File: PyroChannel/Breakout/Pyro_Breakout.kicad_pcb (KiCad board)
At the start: 2 copper layers, 40.6 x 63.5 mm, 17 parts, among them J101 Conn_01x02, J102 Conn_01x05, J103 Conn_01x02, J301 Conn_01x02_Female, J401 Conn_01x02_Female, Q201 IRLML6344TRPBFee, Q301 IRLML6344TRPBFee, Q302 IRLML6344TRPBFee, Q401 IRLML6344TRPBFee, Q402 IRLML6344TRPBFee

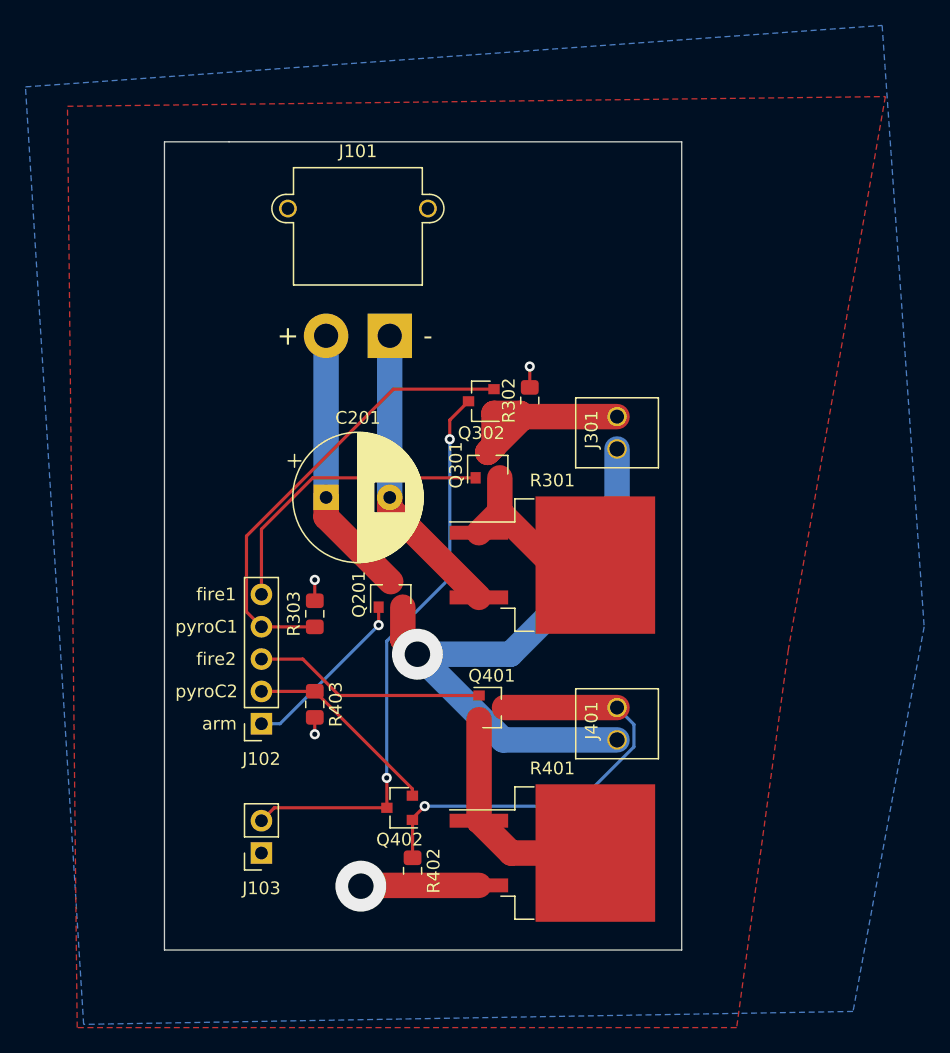
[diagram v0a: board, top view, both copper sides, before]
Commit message: Updated Heirarchichal schematics and breakout to fix checkPyro error
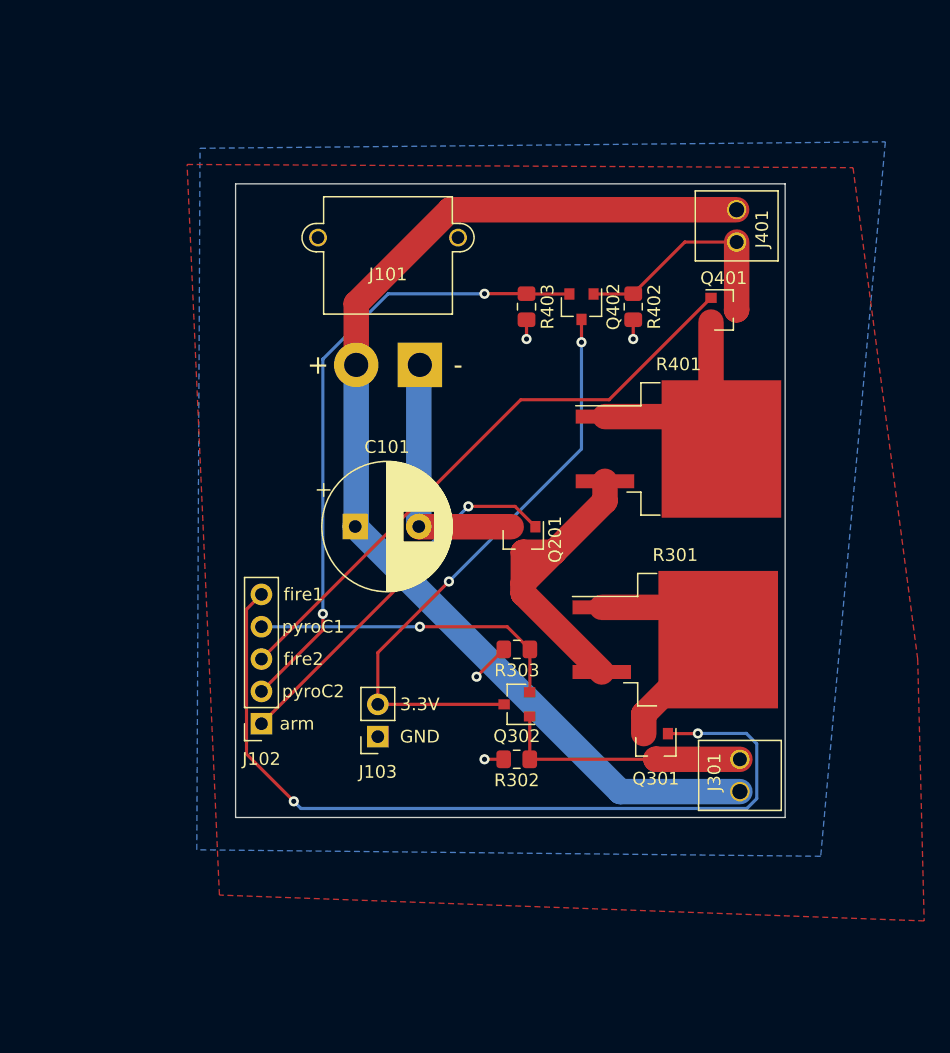
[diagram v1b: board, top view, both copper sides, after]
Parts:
- removed C201: 1mF, PyroChannel:CP_Radial_D10.0mm_P5.00mm
- added C101: 1mF, PyroChannel:CP_Radial_D10.0mm_P5.00mm, F.Cu at (111.5, 75.9)
- moved R402 47.6 mm to (133.3, 58.7)
- moved Q402 41.9 mm to (129.3, 58.7), turned to 270 degrees
- moved J401 40.2 mm to (141.5, 52.3), turned to 270 degrees
- moved Q401 36.2 mm to (140.5, 58.9)
- moved R403 35.4 mm to (125.0, 58.7)
- moved R401 33.3 mm to (136.9, 69.8)
- moved J301 28.6 mm to (141.7, 95.5)
- moved R302 28.2 mm to (124.2, 94.2), turned to 180 degrees
- moved Q301 25.7 mm to (135.1, 93.2), turned to 270 degrees
- moved Q302 24.0 mm to (124.2, 89.9)
- moved R303 16.1 mm to (124.2, 85.6), turned to 180 degrees
- moved J103 12.9 mm to (113.3, 92.5)
- moved R301 11.3 mm to (136.7, 84.8)
- moved Q201 11.3 mm to (124.7, 77.0), turned to 270 degrees
- moved J101 3.29 mm to (116.6, 63.2)
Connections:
- J301 pad 1: /Pyro2/ARM_Voltage -> +BATT
- J401 pad 1: /Pyro2/ARM_Voltage -> +BATT
- Q201 pad 2: /Pyro2/ARM_Voltage -> GND
- Q201 pad 3: +BATT -> /ArmSchematic/FireOut
- R301 pad 2: GND -> /ArmSchematic/FireOut
- R401 pad 2: GND -> /ArmSchematic/FireOut
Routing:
- net +BATT: track 21.4 -> 89.3 mm
- net /Pyro2/ARM_Voltage: track 49.5 -> 0.00 mm, vias 1 -> 0
- net /fire1: track 23.6 -> 66.8 mm, vias 0 -> 2
- net /pyroCorrect2: track 15.6 -> 49.7 mm, vias 0 -> 2
- net /fire2: track 18.3 -> 47.1 mm
- net /ArmSchematic/FireOut: track 0.00 -> 25.8 mm
- net Net-(J401-Pad2): track 35.3 -> 18.3 mm, vias 1 -> 0
- net /arm: track 13.8 -> 29.7 mm, vias 1 -> 2
- net /pyroCorrect1: track 36.0 -> 25.2 mm, vias 0 -> 1
- net GND: track 37.4 -> 27.6 mm
- net Net-(Q301-Pad2): track 14.2 -> 20.0 mm
- net Net-(J301-Pad2): track 17.0 -> 19.9 mm
- net Net-(Q401-Pad2): track 18.1 -> 20.5 mm
- net +3V3: track 44.9 -> 46.8 mm
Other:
- board size 40.6 x 63.5 mm -> 43.2 x 49.8 mm
- board text added: "3.3V"
- board text added: "GND"

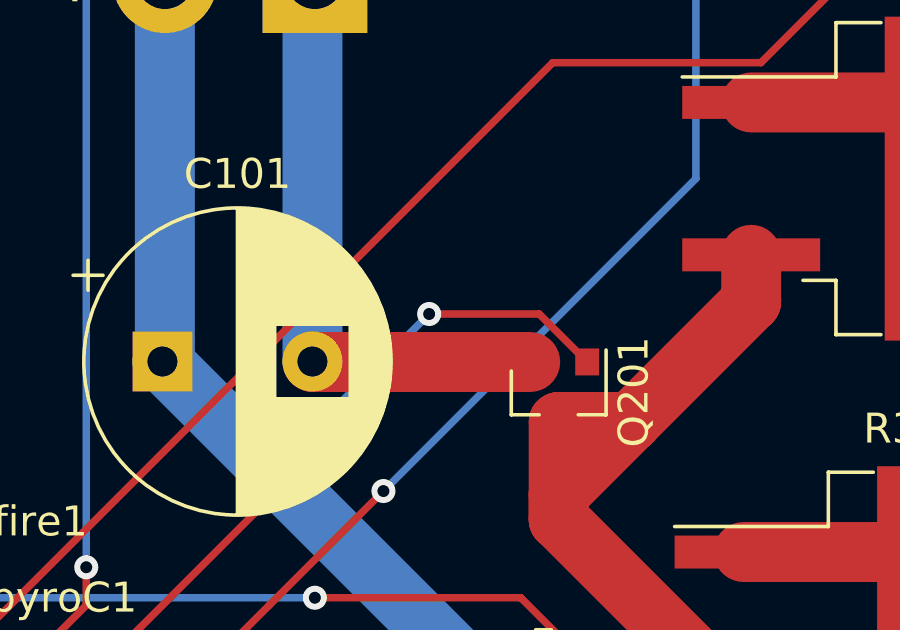
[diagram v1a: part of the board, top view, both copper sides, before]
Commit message: Added pull down to Arming mosfet on pyro channel
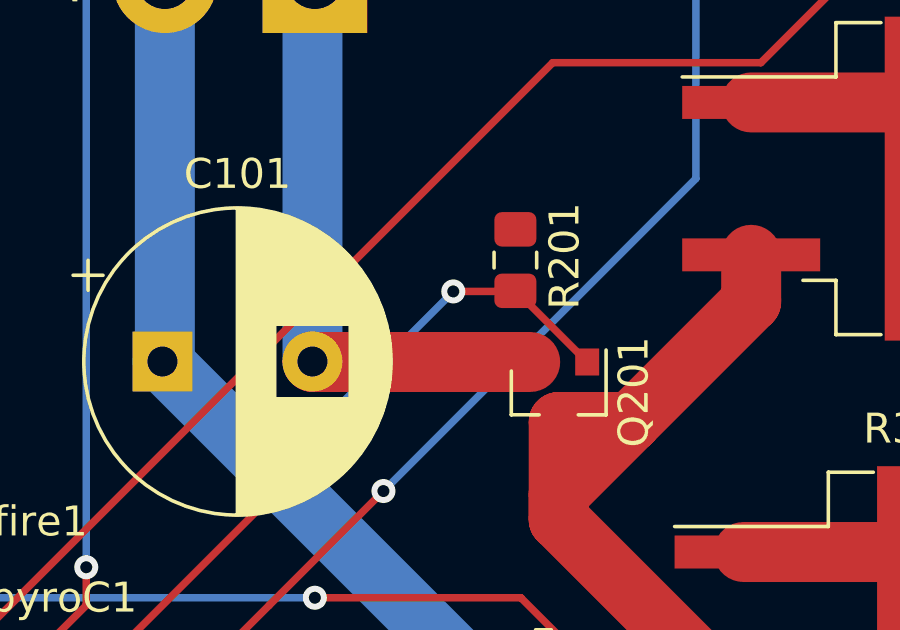
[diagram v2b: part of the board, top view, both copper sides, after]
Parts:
- added R201: 10k, Resistor_SMD:R_0805_2012Metric_Pad1.15x1.40mm_HandSolder, F.Cu at (123.3, 72.6)
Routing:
- net /arm: track 29.7 -> 30.4 mm
